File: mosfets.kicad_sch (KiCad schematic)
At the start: 10 parts, among them Q1 NMOS, Q2 NMOS, Q3 NMOS

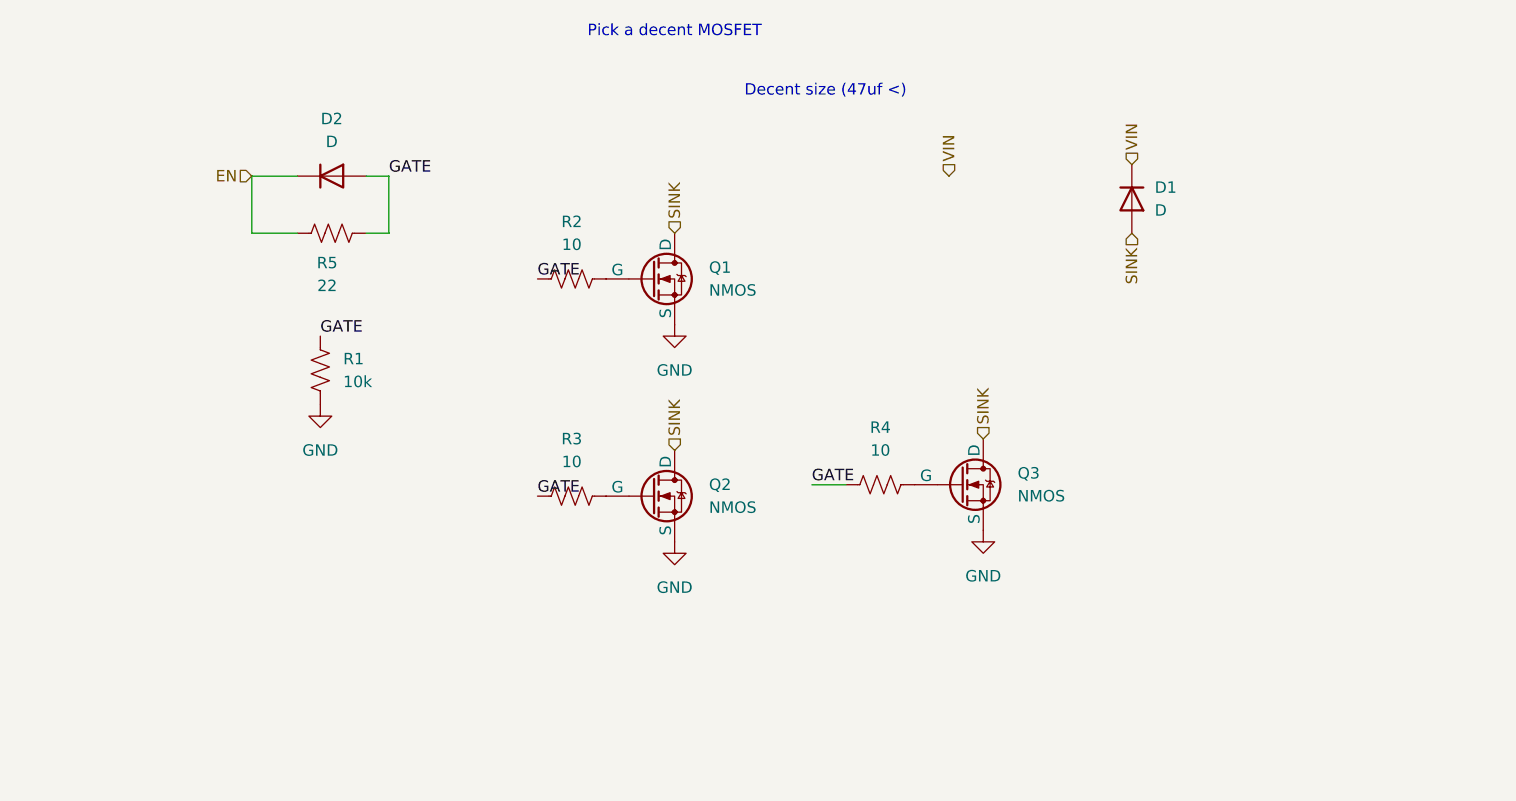
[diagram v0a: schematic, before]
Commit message: changed connectors, cleaned up schematic
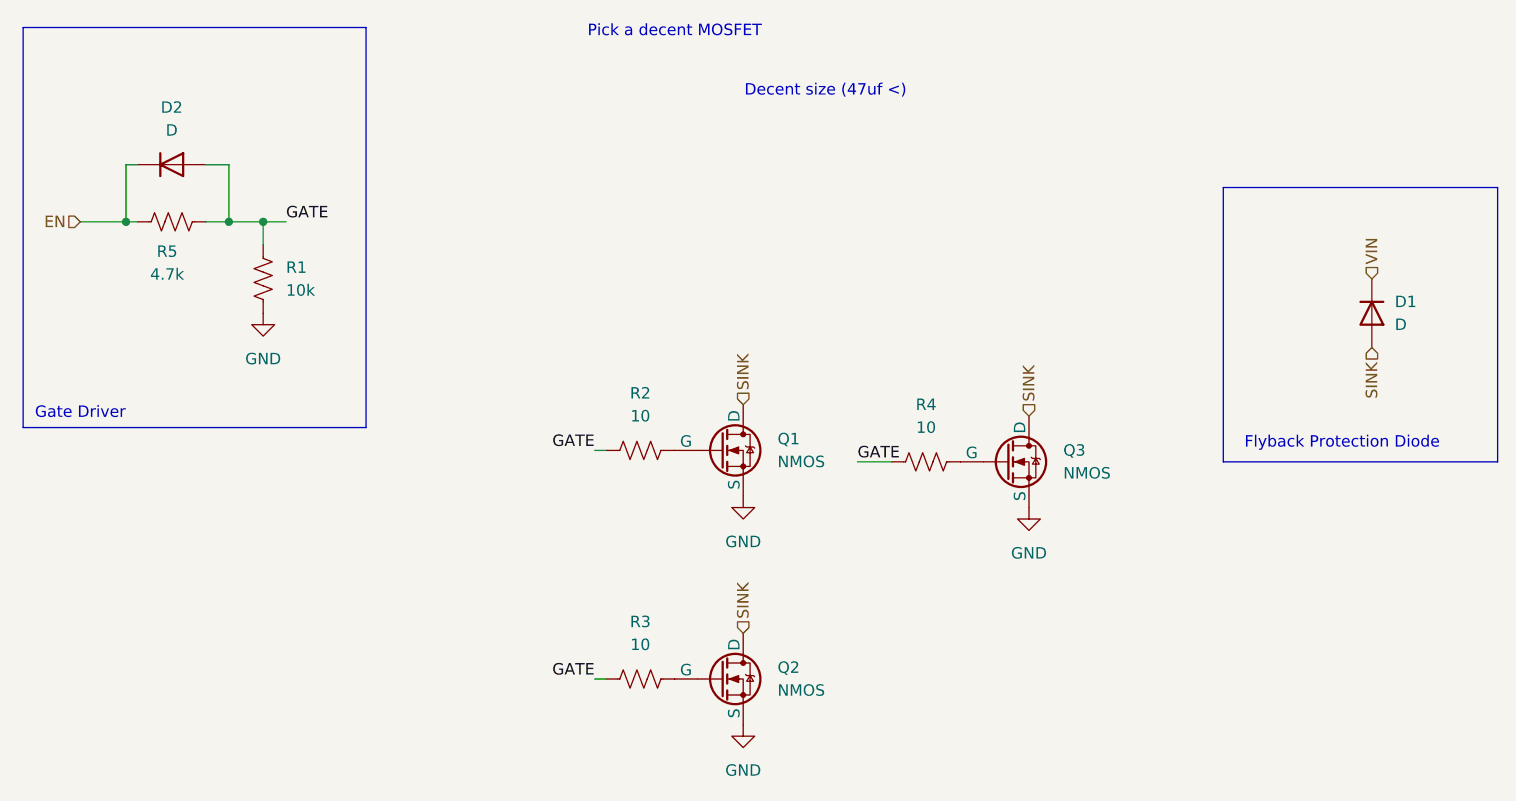
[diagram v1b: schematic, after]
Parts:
- R1, R2, R3, R4: footprint (none) -> Resistor_SMD:R_0805_2012Metric_Pad1.20x1.40mm_HandSolder
- R5: value 22 -> 4.7k; footprint (none) -> Resistor_SMD:R_0805_2012Metric_Pad1.20x1.40mm_HandSolder
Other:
- note added: "Flyback Protection Diode"
- note added: "Gate Driver"
- moved on the sheet: D1, D2, Q1, Q2, Q3, R1, R2, R3, R4, R5
